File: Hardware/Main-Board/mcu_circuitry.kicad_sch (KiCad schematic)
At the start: 3 parts, among them U8 DS3231MZ

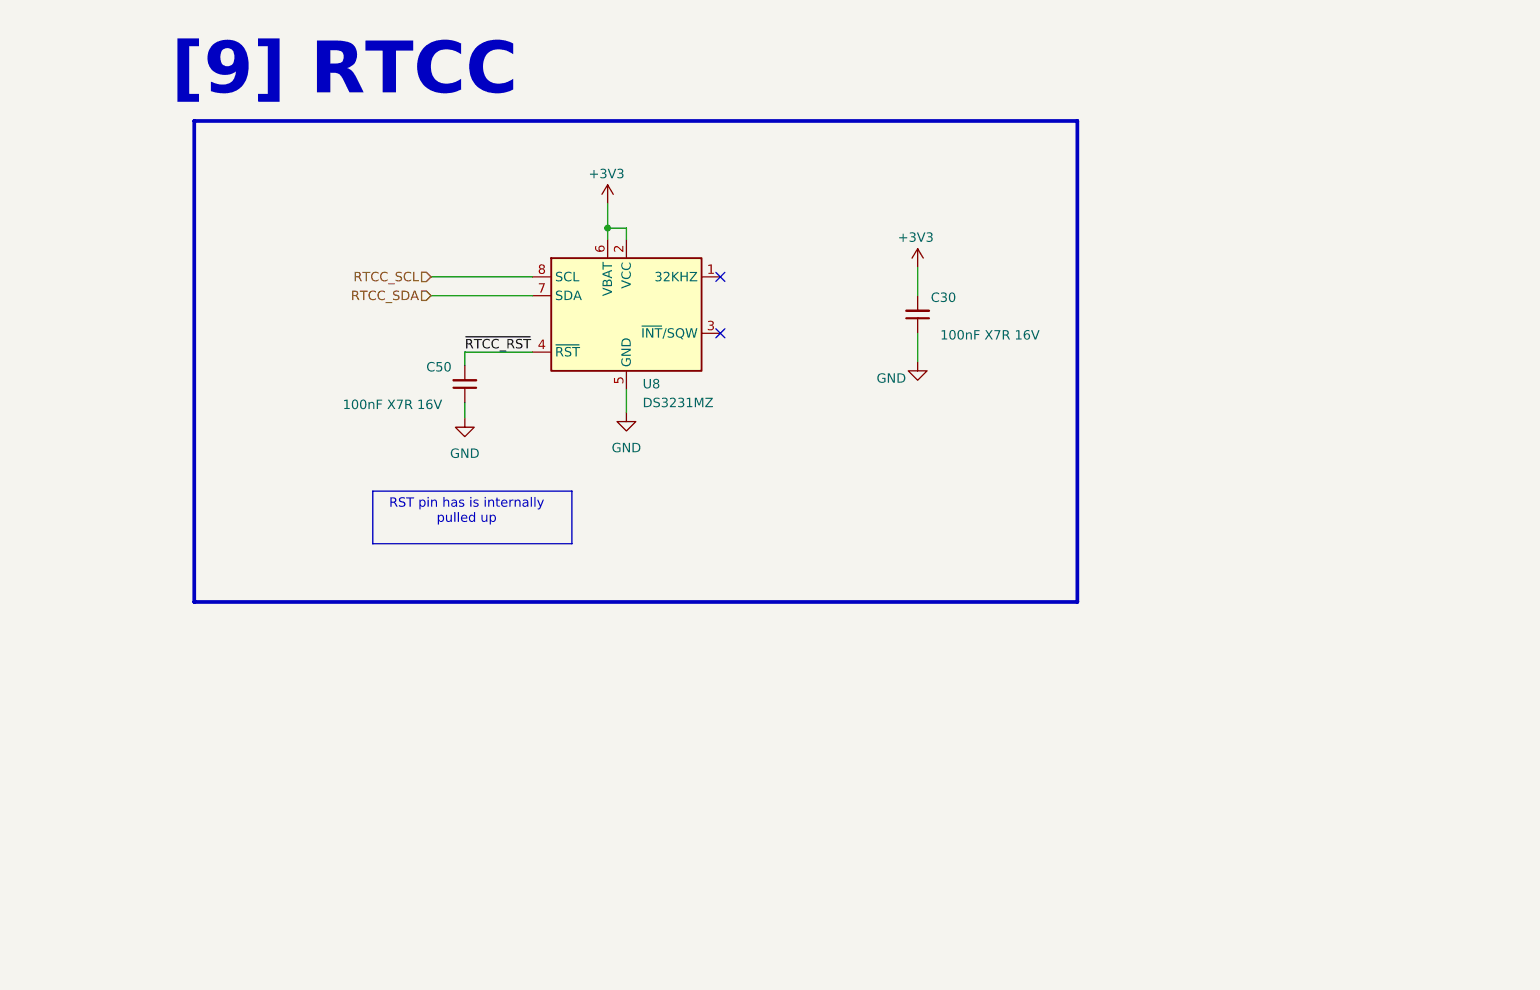
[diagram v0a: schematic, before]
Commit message: Done with main board design, and camera interconnect in progress
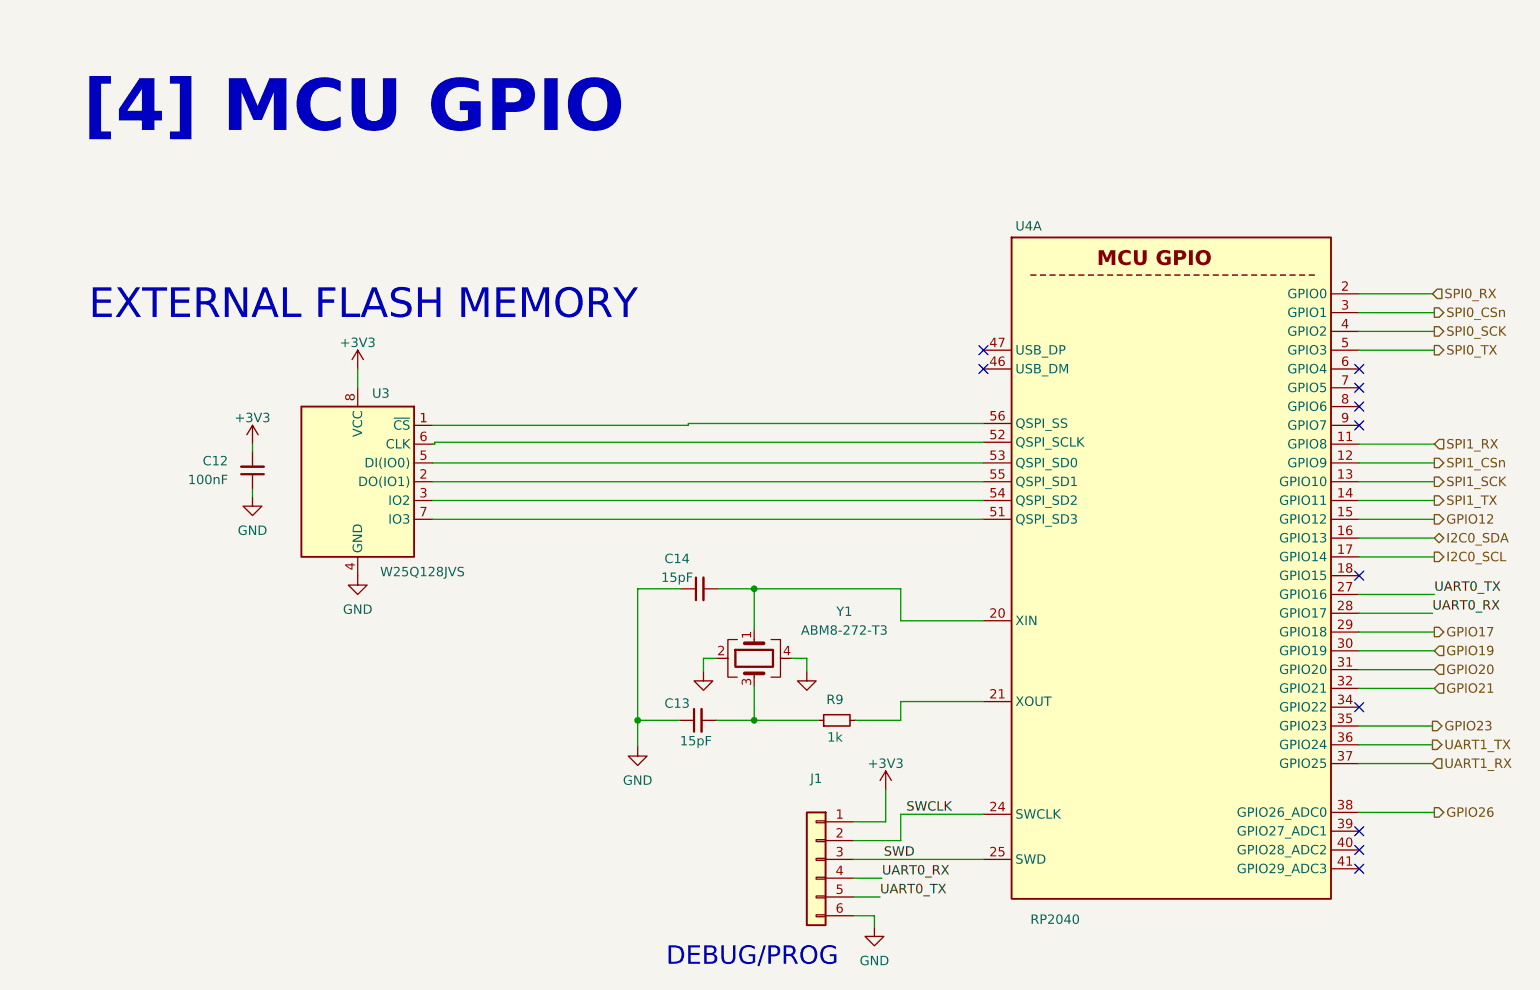
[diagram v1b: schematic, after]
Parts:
- removed C30, C50: 100nF X7R 16V, Capacitor_SMD:C_0402_1005Metric, symbol Device:C_Small
- removed U8: DS3231MZ, Package_SO:SOIC-8_3.9x4.9mm_P1.27mm, symbol Timer_RTC:DS3231MZ
- added C12: 100nF, Capacitor_SMD:C_0402_1005Metric, symbol Device:C_Small
- added C13, C14: 15pF, Capacitor_SMD:C_0402_1005Metric, symbol Device:C_Small
- added J1: Conn_01x06, Connector_PinHeader_2.54mm:PinHeader_2x03_P2.54mm_Vertical, symbol Connector_Generic:Conn_01x06
- added R9: 1k, Resistor_SMD:R_0402_1005Metric, symbol Device:R_Small
- added U3: W25Q128JVS, Package_SO:SOIC-8_5.23x5.23mm_P1.27mm, symbol Memory_Flash:W25Q128JVS
- added U4: RP2040, Package_DFN_QFN:QFN-56-1EP_7x7mm_P0.4mm_EP3.2x3.2mm, symbol MCU_RaspberryPi:RP2040
- added Y1: ABM8-272-T3, ABM8_272_T3:ABM8-272-T3_ABR, symbol Device:Crystal_GND24
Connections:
- net +3V3: now also C12.2, J1.1 (Pin_1), U3.8 (VCC)
- net GND: now also C12.1, C13.1, C14.1, J1.6 (Pin_6), U3.4 (GND), Y1.2, Y1.4
- new net: C13.2, R9.1, Y1.3
- new net: R9.2, U4.21 (XOUT)
- new net: C14.2, U4.20 (XIN), Y1.1
- new net: U3.7 (IO3), U4.51 (QSPI_SD3)
- new net: U3.6 (CLK), U4.52 (QSPI_SCLK)
- new net: U3.5 (DI(IO0)), U4.53 (QSPI_SD0)
- new net: U3.3 (IO2), U4.54 (QSPI_SD2)
- new net: U3.2 (DO(IO1)), U4.55 (QSPI_SD1)
- new net: U3.1 (~{CS}), U4.56 (QSPI_SS)
- new net GPIO12: U4.15 (GPIO12)
- new net GPIO17: U4.29 (GPIO18)
- new net GPIO19: U4.30 (GPIO19)
- new net GPIO20: U4.31 (GPIO20)
- new net GPIO21: U4.32 (GPIO21)
- new net GPIO23: U4.35 (GPIO23)
- new net GPIO26: U4.38 (GPIO26_ADC0)
- new net I2C0_SCL: U4.17 (GPIO14)
- new net I2C0_SDA: U4.16 (GPIO13)
- new net SPI0_CSn: U4.3 (GPIO1)
- new net SPI0_RX: U4.2 (GPIO0)
- new net SPI0_SCK: U4.4 (GPIO2)
- new net SPI0_TX: U4.5 (GPIO3)
- new net SPI1_CSn: U4.12 (GPIO9)
- new net SPI1_RX: U4.11 (GPIO8)
- new net SPI1_SCK: U4.13 (GPIO10)
- new net SPI1_TX: U4.14 (GPIO11)
- new net SWCLK: J1.2 (Pin_2), U4.24 (SWCLK)
- new net SWD: J1.3 (Pin_3), U4.25 (SWD)
- new net UART0_RX: J1.4 (Pin_4), U4.28 (GPIO17)
- new net UART0_TX: J1.5 (Pin_5), U4.27 (GPIO16)
- new net UART1_RX: U4.37 (GPIO25)
- new net UART1_TX: U4.36 (GPIO24)
- no-connect marks 2 -> 11
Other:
- note added: "DEBUG/PROG"
- note added: "EXTERNAL FLASH MEMORY"
- note added: "[4] MCU GPIO"
- note removed: "RST pin has is internally pulled up"
- note removed: "[9] RTCC"
